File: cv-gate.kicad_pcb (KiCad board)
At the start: 2 copper layers, 29.5 x 22.5 mm, 49 parts, among them J1 Conn_01x06_Socket, J2 Conn_01x06_Socket, J3 Conn_02x05_Odd_Even, U2 TL074, U3 TL074, U4 MCP1703Ax-500xxDB

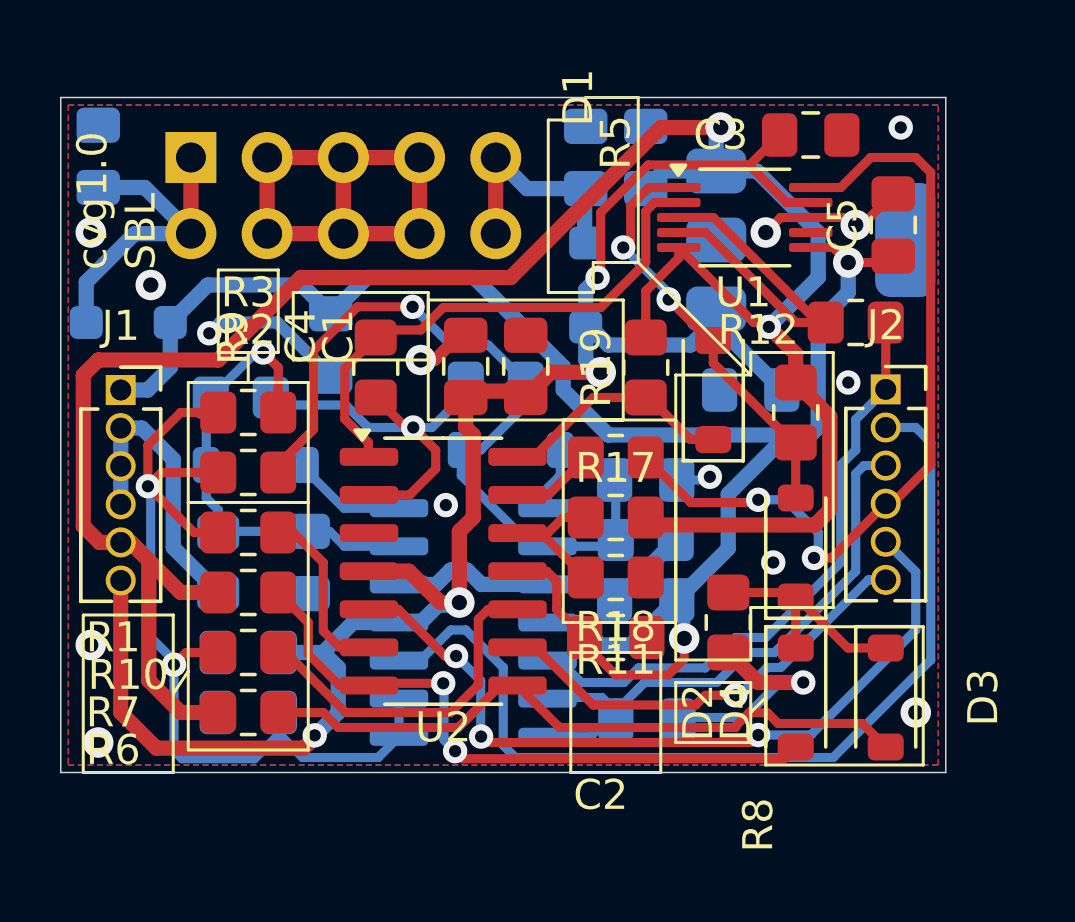
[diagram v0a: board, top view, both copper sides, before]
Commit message: Moved I/O buffering to interface board, add license
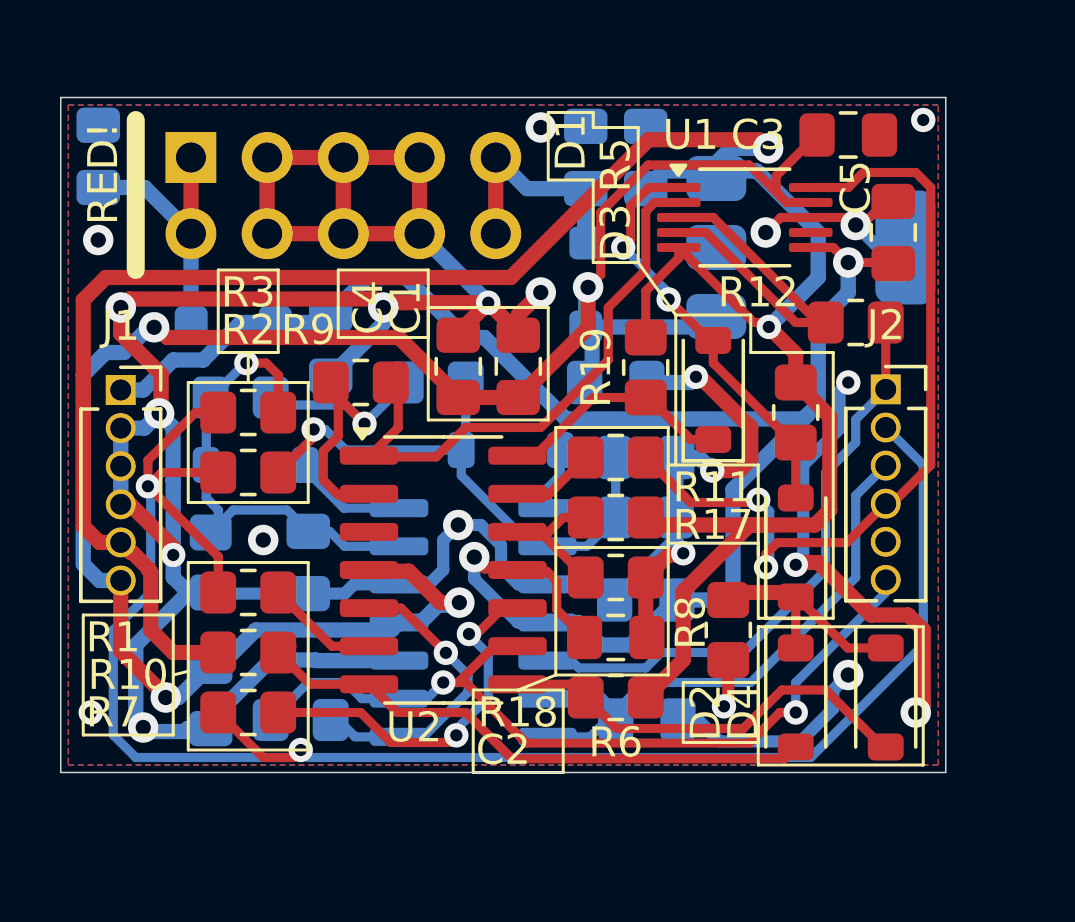
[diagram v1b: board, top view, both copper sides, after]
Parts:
- removed C15: 100pF, Capacitor_SMD:C_0805_2012Metric_Pad1.18x1.45mm_HandSolder
- added R4: 10K, Resistor_SMD:R_0805_2012Metric_Pad1.20x1.40mm_HandSolder, B.Cu at (148.0, 110.8)
- moved R6 12.3 mm to (158.5, 110.0), turned to 180 degrees
- moved C14 4.51 mm to (158.5, 99.5), turned to 180 degrees
- moved D6 3.50 mm to (145.8, 97.5)
- moved R1 2.00 mm to (146.2, 106.5)
- moved R10 2.00 mm to (146.2, 108.5)
- moved R16 2.00 mm to (152.5, 99.5)
- moved R7 2.00 mm to (146.2, 110.5)
- moved C11 1.95 mm to (145.0, 110.0), turned to 90 degrees
- moved C3 1.25 mm to (166.2, 91.2)
- moved C8 0.75 mm to (159.5, 102.0)
- moved R15 0.75 mm to (159.5, 104.0)
- moved R9 0.71 mm to (150.0, 99.5), turned to 0 degrees
- moved C1 0.25 mm to (155.2, 99.0)
- moved C4 0.25 mm to (153.2, 99.0)
- moved C5 0.25 mm to (167.8, 94.5)
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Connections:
- net /CV_OUT_BUFFERED renamed /CV_OUT_RAW
- J2 pad 2: /CV_IN_RAW -> /CV_IN_BUFFERED
- J2 pad 5: /THRESHOLD_NEGATIVE -> unconnected-(J2-Pin_5-Pad5)
- U3 pad 1: /CV_IN_BUFFERED -> /THRESHOLD_NEGATIVE
- U3 pad 2: /CV_IN_BUFFERED -> /THRESHOLD_POSITIVE
- U3 pad 3: /CV_IN_RAW -> GND
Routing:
- net GND: track 60.7 -> 140.1 mm, vias 15 -> 23
- net /CV_IN_RAW: track 31.7 -> 0.00 mm
- net /CV_IN_BUFFERED: track 32.3 -> 60.6 mm
- net /THRESHOLD_NEGATIVE: track 26.1 -> 10.3 mm, vias 3 -> 1
- net /THRESHOLD_POSITIVE: track 14.8 -> 28.4 mm, vias 1 -> 2
- net /POS_COMPARE_RESULT: track 22.3 -> 14.2 mm
- net +12V: track 61.6 -> 69.3 mm
- net /POS_PEAK_RECTIFIED: track 26.2 -> 18.8 mm
- net +5V: track 75.5 -> 81.5 mm
- net /-12V_RAW: track 12.0 -> 9.23 mm
- net Net-(U2B--): track 5.95 -> 3.77 mm
- net -12V: track 61.5 -> 59.3 mm
- net /NEG_COMPARE_RESULT: track 21.5 -> 19.4 mm, vias 2 -> 0
- net Net-(U2C-+): track 11.5 -> 12.8 mm, vias 0 -> 2
- net Net-(U2A--): track 13.7 -> 12.4 mm
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
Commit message: Add bom, 3d model
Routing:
- net GND: track 140.1 -> 140.9 mm
